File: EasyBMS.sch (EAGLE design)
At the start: 147 parts, among them Q1 BSS84LT1G, Q10 BSS84LT1G, Q11 BSS84LT1G, Q12 BSS84LT1G, Q14 BSS84LT1G, Q3 BSS84LT1G, Q4 BSS84LT1G, Q5 BSS84LT1G, Q6 BSS84LT1G, Q7 BSS84LT1G, Q8 BSS84LT1G, Q9 BSS84LT1G

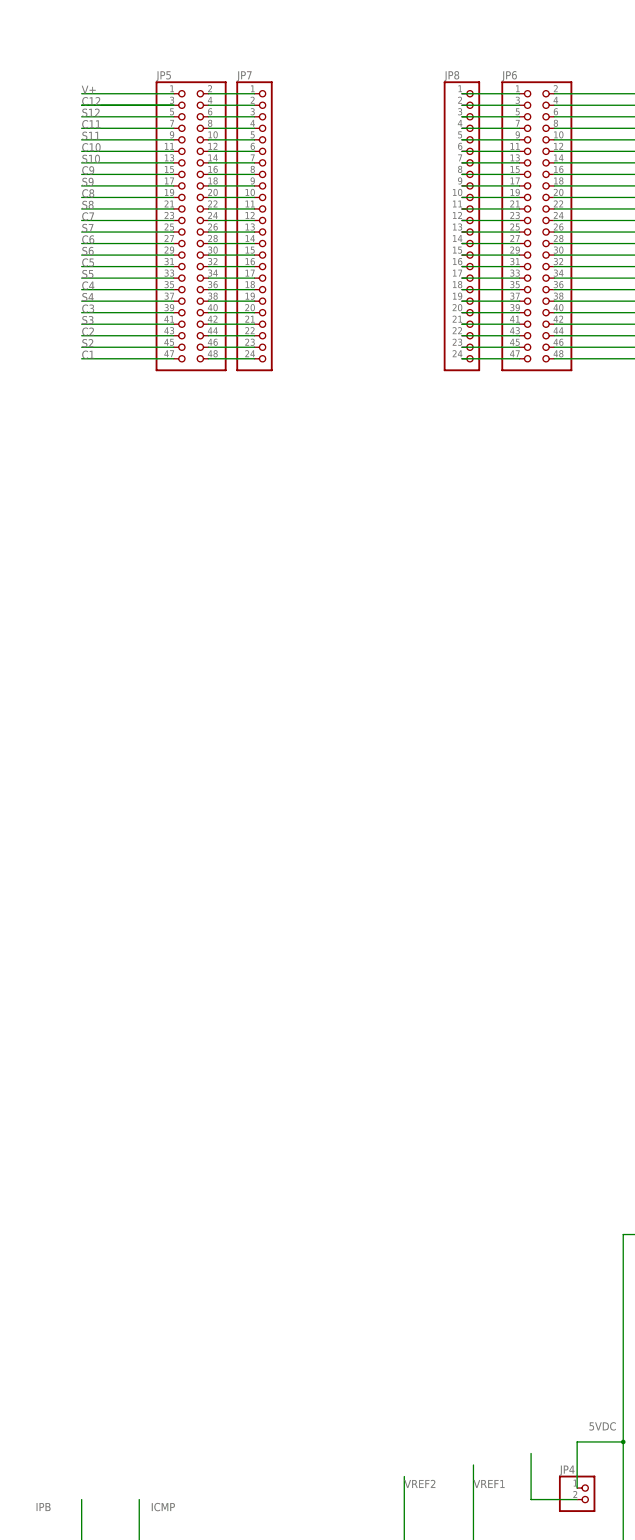
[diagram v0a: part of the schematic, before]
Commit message: supply voltage bug removed
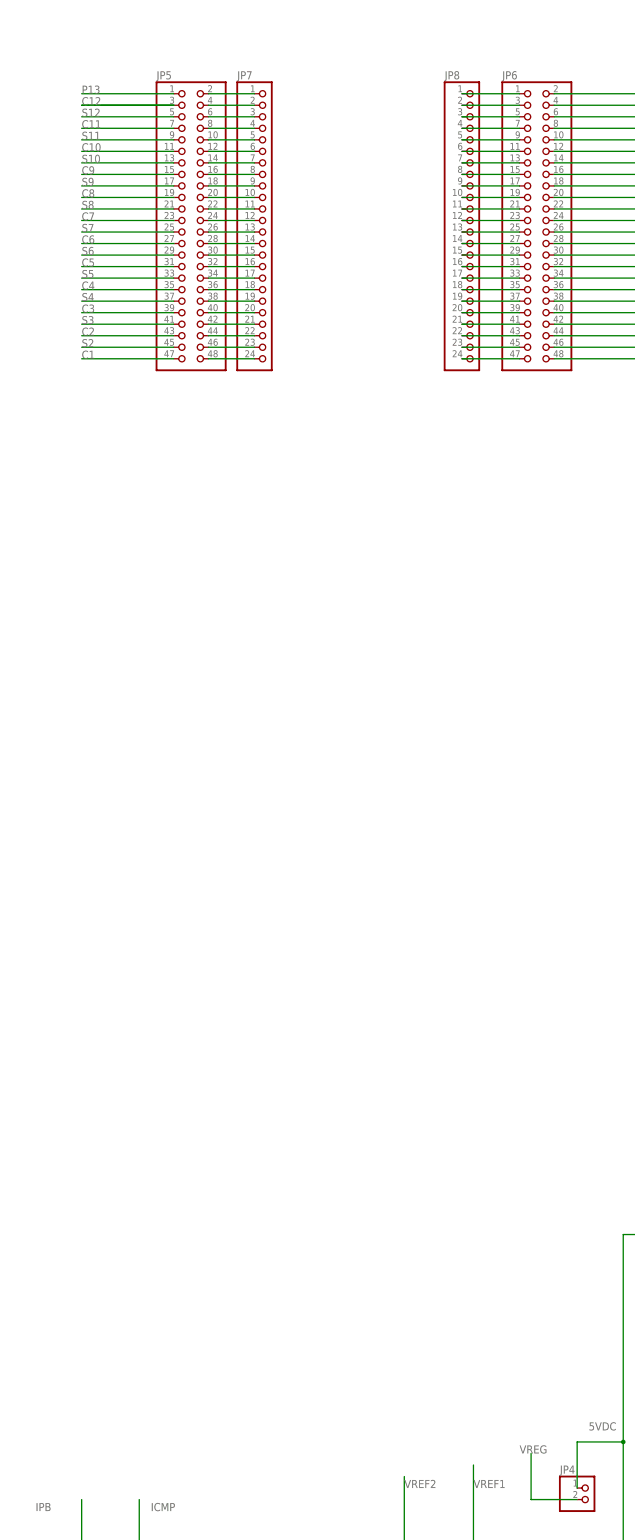
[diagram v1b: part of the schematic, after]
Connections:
- removed net N$106: JP4.2
- removed net V+: JP5.1
- net P13: now also JP5.1
- net VREG: now also JP4.2
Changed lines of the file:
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@@
-</segment>
-</net>
-<net name="N$106" class="0">
-<segment>
-<wire x1="177.8" y1="53.34" x2="177.8" y2="43.18" width="0.1524" layer="91"/>
-<pinref part="JP4" gate="G$1" pin="2"/>
-<wire x1="177.8" y1="43.18" x2="187.96" y2="43.18" width="0.1524" layer="91"/>
 </segment>
 </net>
@@
 <junction x="403.86" y="144.78"/>
 <pinref part="D2" gate="G$1" pin="K"/>
+</segment>
+<segment>
+<wire x1="99.06" y1="353.06" x2="78.74" y2="353.06" width="0.1524" layer="91"/>
+<pinref part="JP5" gate="A" pin="1"/>
+<label x="78.74" y="353.06" size="1.778" layer="95"/>
 </segment>
 </net>
@@
 </segment>
 </net>
-<net name="V+" class="0">
-<segment>
-<wire x1="99.06" y1="353.06" x2="78.74" y2="353.06" width="0.1524" layer="91"/>
-<pinref part="JP5" gate="A" pin="1"/>
-<label x="78.74" y="353.06" size="1.778" layer="95"/>
-</segment>
-</net>
 <net name="IPB" class="0">
 <segment>
@@
 <pinref part="JP6" gate="A" pin="24"/>
 </segment>
-</net>
+<segment>
+<wire x1="177.8" y1="53.34" x2="177.8" y2="43.18" width="0.1524" layer="91"/>
+<pinref part="JP4" gate="G$1" pin="2"/>
+<wire x1="177.8" y1="43.18" x2="187.96" y2="43.18" width="0.1524" layer="91"/>
+<label x="175.26" y="53.34" size="1.778" layer="95"/>
+</segment>
+</net>

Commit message: transistor changed to the type from example BSS308
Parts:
- Q1, Q10, Q11, Q12, Q14, Q3, Q4, Q5, Q6, Q7, Q8, Q9: value BSS84LT1G -> BSS308PEH6327XTSA1; device SamacSys_Parts:BSS84LT1G -> SamacSys_Parts:BSS308PEH6327XTSA1
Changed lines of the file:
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@@
 <part name="JP3" library="pinhead_own" deviceset="PINHD-1X2" device="" package3d_urn="urn:adsk.eagle:package:22435/2"/>
 <part name="JP4" library="pinhead_own" deviceset="PINHD-1X2" device="" package3d_urn="urn:adsk.eagle:package:22435/2"/>
-<part name="Q1" library="SamacSys_Parts" deviceset="BSS84LT1G" device=""/>
+<part name="Q1" library="SamacSys_Parts" deviceset="BSS308PEH6327XTSA1" device=""/>
 <part name="R9" library="rcl" library_urn="urn:adsk.eagle:library:334" deviceset="R-EU_" device="R1206" package3d_urn="urn:adsk.eagle:package:23540/2" value="10R0"/>
 <part name="R13" library="rcl" library_urn="urn:adsk.eagle:library:334" deviceset="R-EU_" device="R0402" package3d_urn="urn:adsk.eagle:package:23547/1" value="3.3k"/>
@@
 <part name="R12" library="rcl" library_urn="urn:adsk.eagle:library:334" deviceset="R-EU_" device="R1206" package3d_urn="urn:adsk.eagle:package:23540/2" value="10R0"/>
 <part name="R14" library="rcl" library_urn="urn:adsk.eagle:library:334" deviceset="R-EU_" device="R1206" package3d_urn="urn:adsk.eagle:package:23540/2" value="10R0"/>
-<part name="Q3" library="SamacSys_Parts" deviceset="BSS84LT1G" device=""/>
+<part name="Q3" library="SamacSys_Parts" deviceset="BSS308PEH6327XTSA1" device=""/>
 <part name="R20" library="rcl" library_urn="urn:adsk.eagle:library:334" deviceset="R-EU_" device="R1206" package3d_urn="urn:adsk.eagle:package:23540/2" value="10R0"/>
 <part name="R21" library="rcl" library_urn="urn:adsk.eagle:library:334" deviceset="R-EU_" device="R0402" package3d_urn="urn:adsk.eagle:package:23547/1" value="3.3k"/>
@@
 <part name="R24" library="rcl" library_urn="urn:adsk.eagle:library:334" deviceset="R-EU_" device="R1206" package3d_urn="urn:adsk.eagle:package:23540/2" value="10R0"/>
 <part name="R25" library="rcl" library_urn="urn:adsk.eagle:library:334" deviceset="R-EU_" device="R1206" package3d_urn="urn:adsk.eagle:package:23540/2" value="10R0"/>
-<part name="Q4" library="SamacSys_Parts" deviceset="BSS84LT1G" device=""/>
+<part name="Q4" library="SamacSys_Parts" deviceset="BSS308PEH6327XTSA1" device=""/>
 <part name="R26" library="rcl" library_urn="urn:adsk.eagle:library:334" deviceset="R-EU_" device="R1206" package3d_urn="urn:adsk.eagle:package:23540/2" value="10R0"/>
 <part name="R27" library="rcl" library_urn="urn:adsk.eagle:library:334" deviceset="R-EU_" device="R0402" package3d_urn="urn:adsk.eagle:package:23547/1" value="3.3k"/>
@@
 <part name="R30" library="rcl" library_urn="urn:adsk.eagle:library:334" deviceset="R-EU_" device="R1206" package3d_urn="urn:adsk.eagle:package:23540/2" value="10R0"/>
 <part name="R31" library="rcl" library_urn="urn:adsk.eagle:library:334" deviceset="R-EU_" device="R1206" package3d_urn="urn:adsk.eagle:package:23540/2" value="10R0"/>
-<part name="Q5" library="SamacSys_Parts" deviceset="BSS84LT1G" device=""/>
+<part name="Q5" library="SamacSys_Parts" deviceset="BSS308PEH6327XTSA1" device=""/>
 <part name="R32" library="rcl" library_urn="urn:adsk.eagle:library:334" deviceset="R-EU_" device="R1206" package3d_urn="urn:adsk.eagle:package:23540/2" value="10R0"/>
 <part name="R33" library="rcl" library_urn="urn:adsk.eagle:library:334" deviceset="R-EU_" device="R0402" package3d_urn="urn:adsk.eagle:package:23547/1" value="3.3k"/>
@@
 <part name="R36" library="rcl" library_urn="urn:adsk.eagle:library:334" deviceset="R-EU_" device="R1206" package3d_urn="urn:adsk.eagle:package:23540/2" value="10R0"/>
 <part name="R37" library="rcl" library_urn="urn:adsk.eagle:library:334" deviceset="R-EU_" device="R1206" package3d_urn="urn:adsk.eagle:package:23540/2" value="10R0"/>
-<part name="Q6" library="SamacSys_Parts" deviceset="BSS84LT1G" device=""/>
+<part name="Q6" library="SamacSys_Parts" deviceset="BSS308PEH6327XTSA1" device=""/>
 <part name="R38" library="rcl" library_urn="urn:adsk.eagle:library:334" deviceset="R-EU_" device="R1206" package3d_urn="urn:adsk.eagle:package:23540/2" value="10R0"/>
 <part name="R39" library="rcl" library_urn="urn:adsk.eagle:library:334" deviceset="R-EU_" device="R0402" package3d_urn="urn:adsk.eagle:package:23547/1" value="3.3k"/>
@@
 <part name="R42" library="rcl" library_urn="urn:adsk.eagle:library:334" deviceset="R-EU_" device="R1206" package3d_urn="urn:adsk.eagle:package:23540/2" value="10R0"/>
 <part name="R43" library="rcl" library_urn="urn:adsk.eagle:library:334" deviceset="R-EU_" device="R1206" package3d_urn="urn:adsk.eagle:package:23540/2" value="10R0"/>
-<part name="Q7" library="SamacSys_Parts" deviceset="BSS84LT1G" device=""/>
+<part name="Q7" library="SamacSys_Parts" deviceset="BSS308PEH6327XTSA1" device=""/>
 <part name="R44" library="rcl" library_urn="urn:adsk.eagle:library:334" deviceset="R-EU_" device="R1206" package3d_urn="urn:adsk.eagle:package:23540/2" value="10R0"/>
 <part name="R45" library="rcl" library_urn="urn:adsk.eagle:library:334" deviceset="R-EU_" device="R0402" package3d_urn="urn:adsk.eagle:package:23547/1" value="3.3k"/>
@@
 <part name="R48" library="rcl" library_urn="urn:adsk.eagle:library:334" deviceset="R-EU_" device="R1206" package3d_urn="urn:adsk.eagle:package:23540/2" value="10R0"/>
 <part name="R49" library="rcl" library_urn="urn:adsk.eagle:library:334" deviceset="R-EU_" device="R1206" package3d_urn="urn:adsk.eagle:package:23540/2" value="10R0"/>
-<part name="Q8" library="SamacSys_Parts" deviceset="BSS84LT1G" device=""/>
+<part name="Q8" library="SamacSys_Parts" deviceset="BSS308PEH6327XTSA1" device=""/>
 <part name="R50" library="rcl" library_urn="urn:adsk.eagle:library:334" deviceset="R-EU_" device="R1206" package3d_urn="urn:adsk.eagle:package:23540/2" value="10R0"/>
 <part name="R51" library="rcl" library_urn="urn:adsk.eagle:library:334" deviceset="R-EU_" device="R0402" package3d_urn="urn:adsk.eagle:package:23547/1" value="3.3k"/>
@@
 <part name="R70" library="rcl" library_urn="urn:adsk.eagle:library:334" deviceset="R-EU_" device="R1206" package3d_urn="urn:adsk.eagle:package:23540/2" value="10R0"/>
 <part name="R71" library="rcl" library_urn="urn:adsk.eagle:library:334" deviceset="R-EU_" device="R1206" package3d_urn="urn:adsk.eagle:package:23540/2" value="10R0"/>
-<part name="Q10" library="SamacSys_Parts" deviceset="BSS84LT1G" device=""/>
+<part name="Q10" library="SamacSys_Parts" deviceset="BSS308PEH6327XTSA1" device=""/>
 <part name="R72" library="rcl" library_urn="urn:adsk.eagle:library:334" deviceset="R-EU_" device="R1206" package3d_urn="urn:adsk.eagle:package:23540/2" value="10R0"/>
 <part name="R73" library="rcl" library_urn="urn:adsk.eagle:library:334" deviceset="R-EU_" device="R0402" package3d_urn="urn:adsk.eagle:package:23547/1" value="3.3k"/>
@@
 <part name="R83" library="rcl" library_urn="urn:adsk.eagle:library:334" deviceset="R-EU_" device="R1206" package3d_urn="urn:adsk.eagle:package:23540/2" value="10R0"/>
 <part name="R84" library="rcl" library_urn="urn:adsk.eagle:library:334" deviceset="R-EU_" device="R1206" package3d_urn="urn:adsk.eagle:package:23540/2" value="10R0"/>
-<part name="Q12" library="SamacSys_Parts" deviceset="BSS84LT1G" device=""/>
+<part name="Q12" library="SamacSys_Parts" deviceset="BSS308PEH6327XTSA1" device=""/>
 <part name="R85" library="rcl" library_urn="urn:adsk.eagle:library:334" deviceset="R-EU_" device="R1206" package3d_urn="urn:adsk.eagle:package:23540/2" value="10R0"/>
 <part name="R86" library="rcl" library_urn="urn:adsk.eagle:library:334" deviceset="R-EU_" device="R0402" package3d_urn="urn:adsk.eagle:package:23547/1" value="3.3k"/>
@@
 <part name="R95" library="rcl" library_urn="urn:adsk.eagle:library:334" deviceset="R-EU_" device="R1206" package3d_urn="urn:adsk.eagle:package:23540/2" value="10R0"/>
 <part name="R96" library="rcl" library_urn="urn:adsk.eagle:library:334" deviceset="R-EU_" device="R1206" package3d_urn="urn:adsk.eagle:package:23540/2" value="10R0"/>
-<part name="Q14" library="SamacSys_Parts" deviceset="BSS84LT1G" device=""/>
+<part name="Q14" library="SamacSys_Parts" deviceset="BSS308PEH6327XTSA1" device=""/>
 <part name="R97" library="rcl" library_urn="urn:adsk.eagle:library:334" deviceset="R-EU_" device="R1206" package3d_urn="urn:adsk.eagle:package:23540/2" value="10R0"/>
 <part name="R98" library="rcl" library_urn="urn:adsk.eagle:library:334" deviceset="R-EU_" device="R0402" package3d_urn="urn:adsk.eagle:package:23547/1" value="3.3k"/>
@@
 <part name="R64" library="rcl" library_urn="urn:adsk.eagle:library:334" deviceset="R-EU_" device="R1206" package3d_urn="urn:adsk.eagle:package:23540/2" value="10R0"/>
 <part name="R65" library="rcl" library_urn="urn:adsk.eagle:library:334" deviceset="R-EU_" device="R1206" package3d_urn="urn:adsk.eagle:package:23540/2" value="10R0"/>
-<part name="Q9" library="SamacSys_Parts" deviceset="BSS84LT1G" device=""/>
+<part name="Q9" library="SamacSys_Parts" deviceset="BSS308PEH6327XTSA1" device=""/>
 <part name="R66" library="rcl" library_urn="urn:adsk.eagle:library:334" deviceset="R-EU_" device="R1206" package3d_urn="urn:adsk.eagle:package:23540/2" value="10R0"/>
 <part name="R67" library="rcl" library_urn="urn:adsk.eagle:library:334" deviceset="R-EU_" device="R0402" package3d_urn="urn:adsk.eagle:package:23547/1" value="3.3k"/>
@@
 <part name="R76" library="rcl" library_urn="urn:adsk.eagle:library:334" deviceset="R-EU_" device="R1206" package3d_urn="urn:adsk.eagle:package:23540/2" value="10R0"/>
 <part name="R77" library="rcl" library_urn="urn:adsk.eagle:library:334" deviceset="R-EU_" device="R1206" package3d_urn="urn:adsk.eagle:package:23540/2" value="10R0"/>
-<part name="Q11" library="SamacSys_Parts" deviceset="BSS84LT1G" device=""/>
+<part name="Q11" library="SamacSys_Parts" deviceset="BSS308PEH6327XTSA1" device=""/>
 <part name="R78" library="rcl" library_urn="urn:adsk.eagle:library:334" deviceset="R-EU_" device="R1206" package3d_urn="urn:adsk.eagle:package:23540/2" value="10R0"/>
 <part name="R79" library="rcl" library_urn="urn:adsk.eagle:library:334" deviceset="R-EU_" device="R0402" package3d_urn="urn:adsk.eagle:package:23547/1" value="3.3k"/>
